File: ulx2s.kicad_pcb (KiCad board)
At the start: 4 copper layers, 35.6 x 61 mm, 27 parts, among them J1 Conn_01x24, J2 Conn_01x24, J3 Micro_SD_Card_Det, J4 USB_OTG, J5 Conn_01x06, J6 Audio-Jack-5, SW1 SW_Push, SW2 SW_Push, SW3 SW_Push, SW4 SW_Push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

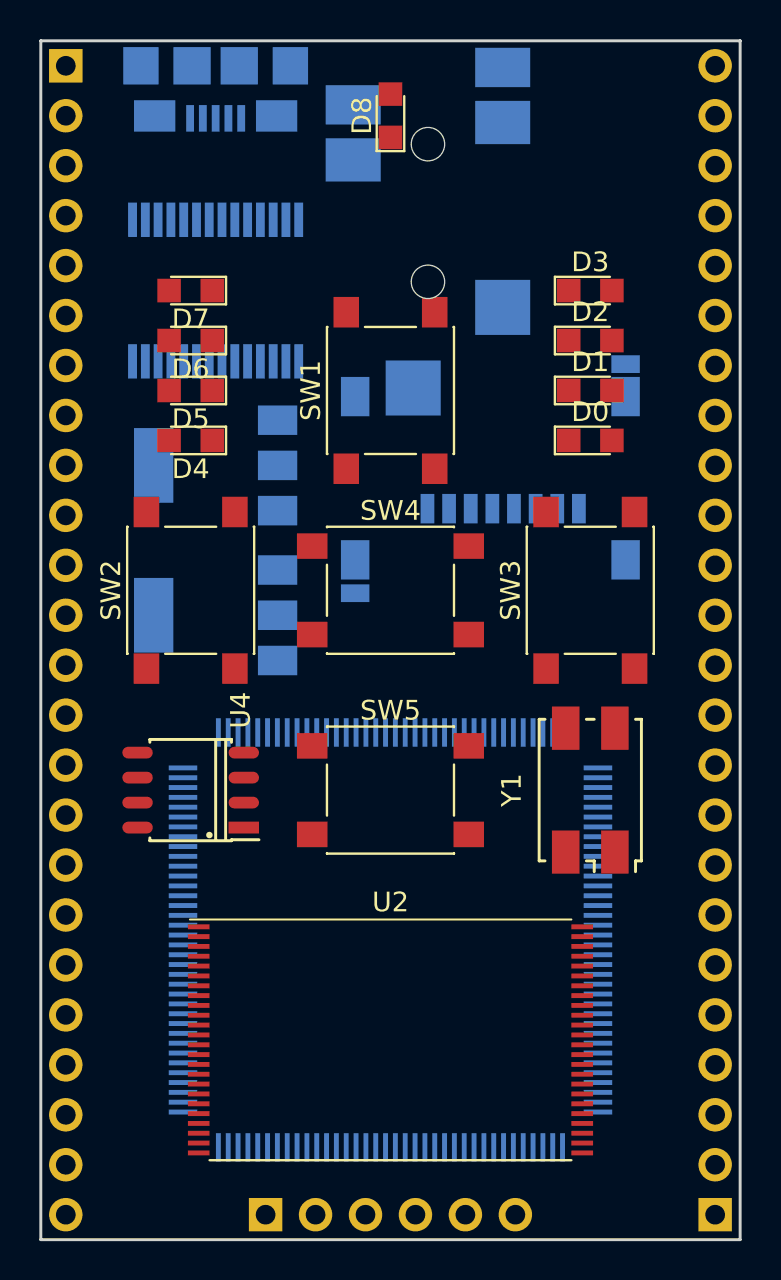
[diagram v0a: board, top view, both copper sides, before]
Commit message: moving components around to better fit
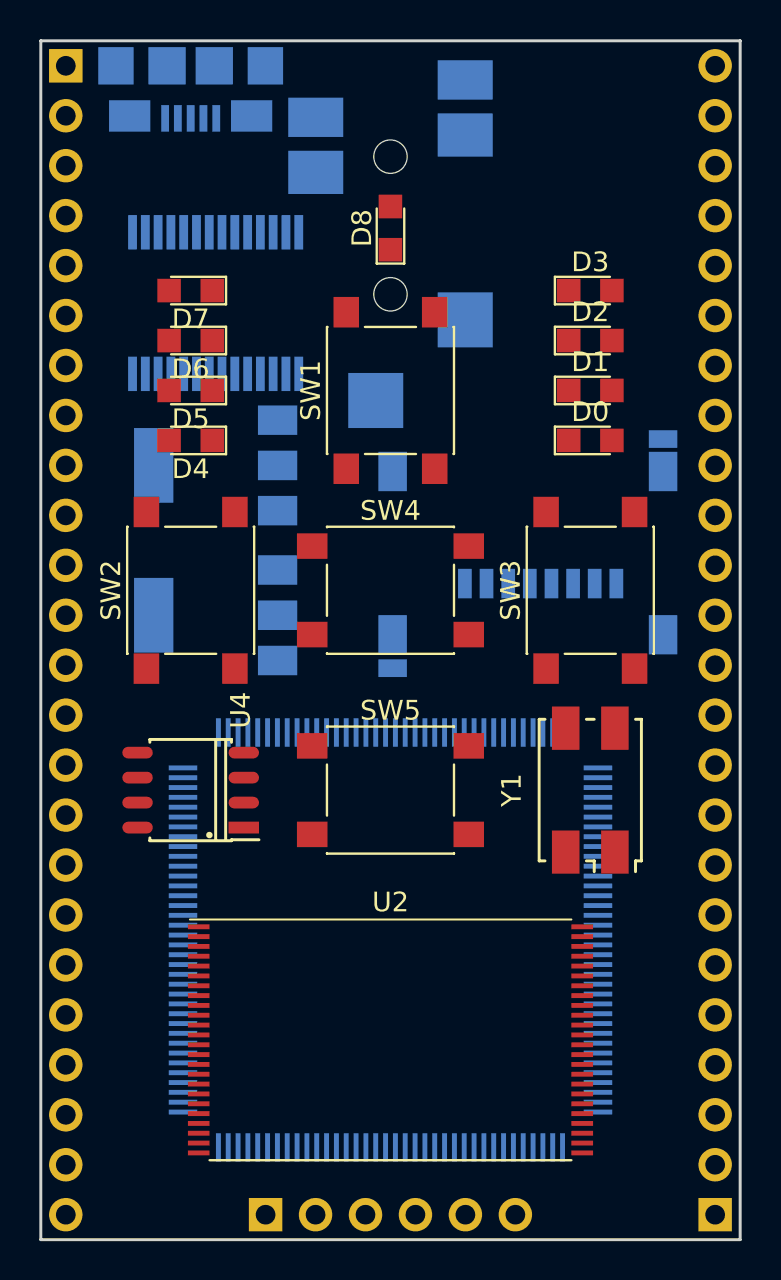
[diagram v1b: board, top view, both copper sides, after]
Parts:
- moved D8 5.72 mm to (158.8, 90.8)
- moved J3 4.26 mm to (165.7, 106.7)
- moved J6 2.01 mm to (158.8, 90.2)
- moved J4 1.27 mm to (148.6, 82.5)
- moved U3 0.63 mm to (149.9, 94.6)
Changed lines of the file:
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@@
   )
   (module micro-sd:SCHD3A100 (layer B.Cu)
-    (at 163.83 102.87 270)
+    (at 165.735 106.68 270)
     (descr "Micro SD card slot SCHD3A0100 from ALPS or ON-STARS")
     (tags "Micro SD SCHD3A0100")
@@
   )
   (module usb_otg:USB-MICRO-B-FCI-10118192-0001LF (layer B.Cu)
-    (at 149.86 82.55)
+    (at 148.59 82.55)
     (fp_text reference J4 (at 0 4.2) (layer B.SilkS)
       (effects (font (size 0.7 0.7) (thickness 0.15)) (justify mirror))
@@
   )
   (module LEDs:LED_0805 (layer F.Cu)
-    (at 158.75 85.09 90)
+    (at 158.75 90.805 90)
     (descr "LED 0805 smd package")
     (tags "LED led 0805 SMD smd SMT smt smdled SMDLED smtled SMTLED")
@@
   )
   (module Housings_SSOP:SSOP-28_5.3x10.2mm_Pitch0.65mm (layer B.Cu)
-    (at 149.86 93.98 90)
+    (at 149.86 94.615 90)
     (descr "28-Lead Plastic Shrink Small Outline (SS)-5.30 mm Body [SSOP] (see Microchip Packaging Specification 00000049BS.pdf)")
     (tags "SSOP 0.65")
     (attr smd)
-    (fp_text reference U3 (at 0 6.25 90) (layer B.SilkS)
+    (fp_text reference U3 (at 0 -5.715 90) (layer B.SilkS)
       (effects (font (size 1 1) (thickness 0.15)) (justify mirror))
     )
@@
   )
   (module audio-jack:CUI_SJ-43516-SMT (layer B.Cu)
-    (at 160.655 89.535 180)
+    (at 158.75 90.17 180)
     (descr "CUI 6-pin audio jack SMT")
     (tags "audio jack")

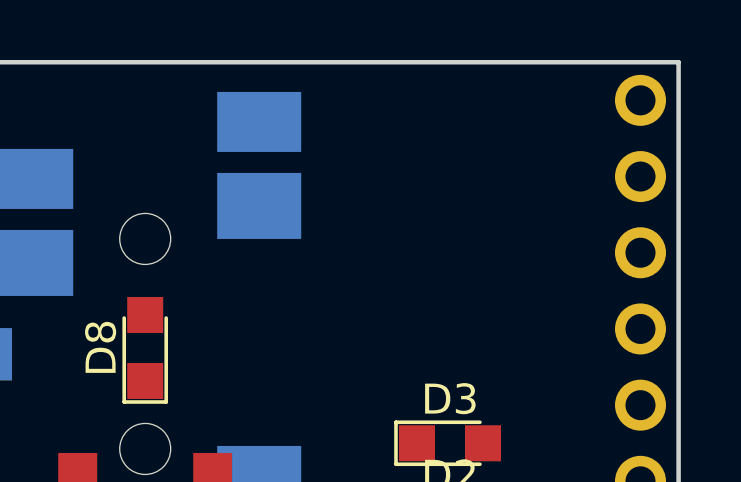
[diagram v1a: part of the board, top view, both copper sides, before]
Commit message: micro hdmi connector
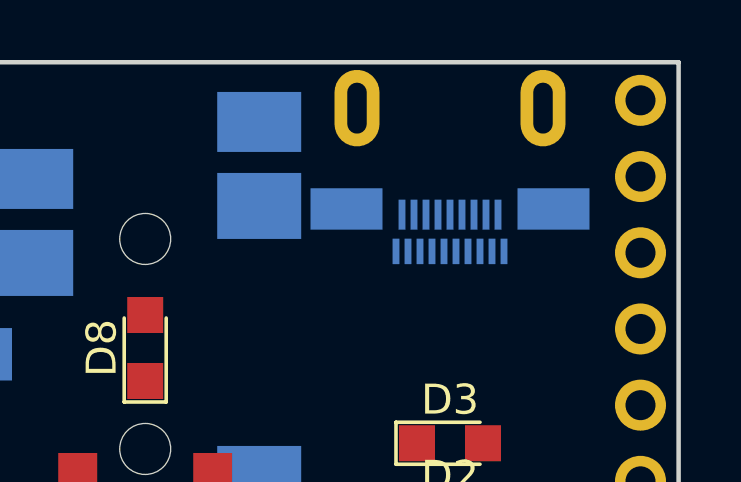
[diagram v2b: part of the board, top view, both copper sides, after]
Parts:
- added P1: MICRO-HDMI-D, micro-hdmi-d:MICRO-HDMI-D, B.Cu at (168.9, 81.1)
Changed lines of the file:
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@@
     (tracks 0)
     (zones 0)
-    (modules 27)
+    (modules 28)
     (nets 13)
   )
@@
       (clearance 0.4))
   )
+  (module micro-hdmi-d:MICRO-HDMI-D (layer B.Cu)
+    (at 168.91 81.11)
+    (attr smd)
+    (fp_text reference P1 (at -0.025 3.125) (layer B.SilkS)
+      (effects (font (size 0.3 0.3) (thickness 0.075)) (justify mirror))
+    )
+    (fp_text value MICRO-HDMI-D (at 0 1.6) (layer B.SilkS)
+      (effects (font (size 0.3 0.3) (thickness 0.075)) (justify mirror))
+    )
+    (fp_line (start -3.3 0) (end -3.3 -0.7) (layer B.SilkS) (width 0.001))
+    (fp_line (start -3.3 -0.7) (end 3.3 -0.7) (layer B.SilkS) (width 0.001))
+    (fp_line (start 3.3 -0.7) (end 3.3 0) (layer B.SilkS) (width 0.001))
+    (fp_line (start -3.3 0) (end -3.3 6.8) (layer B.SilkS) (width 0.001))
+    (fp_line (start -3.3 6.8) (end 3.3 6.8) (layer B.SilkS) (width 0.001))
+    (fp_line (start 3.3 6.8) (end 3.3 0) (layer B.SilkS) (width 0.001))
+    (fp_line (start 3.3 0) (end -3.3 0) (layer B.SilkS) (width 0.001))
+    (pad 1 smd rect (at 1.8 6.475) (size 0.23 0.85) (layers B.Cu B.Paste B.Mask))
+    (pad 3 smd rect (at 1.4 6.475) (size 0.23 0.85) (layers B.Cu B.Paste B.Mask))
+    (pad 5 smd rect (at 1 6.475) (size 0.23 0.85) (layers B.Cu B.Paste B.Mask))
+    (pad 7 smd rect (at 0.6 6.475) (size 0.23 0.85) (layers B.Cu B.Paste B.Mask))
+    (pad 9 smd rect (at 0.2 6.475) (size 0.23 0.85) (layers B.Cu B.Paste B.Mask))
+    (pad 11 smd rect (at -0.2 6.475) (size 0.23 0.85) (layers B.Cu B.Paste B.Mask))
+    (pad 13 smd rect (at -0.6 6.475) (size 0.23 0.85) (layers B.Cu B.Paste B.Mask))
+    (pad 15 smd rect (at -1 6.475) (size 0.23 0.85) (layers B.Cu B.Paste B.Mask))
+    (pad 17 smd rect (at -1.4 6.475) (size 0.23 0.85) (layers B.Cu B.Paste B.Mask))
+    (pad 19 smd rect (at -1.8 6.475) (size 0.23 0.85) (layers B.Cu B.Paste B.Mask))
+    (pad 2 smd rect (at 1.6 5.25) (size 0.23 1) (layers B.Cu B.Paste B.Mask))
+    (pad 4 smd rect (at 1.2 5.25) (size 0.23 1) (layers B.Cu B.Paste B.Mask))
+    (pad 6 smd rect (at 0.8 5.25) (size 0.23 1) (layers B.Cu B.Paste B.Mask))
+    (pad 8 smd rect (at 0.4 5.25) (size 0.23 1) (layers B.Cu B.Paste B.Mask))
+    (pad 10 smd rect (at 0 5.25) (size 0.23 1) (layers B.Cu B.Paste B.Mask))
+    (pad 12 smd rect (at -0.4 5.25) (size 0.23 1) (layers B.Cu B.Paste B.Mask))
+    (pad 14 smd rect (at -0.8 5.25) (size 0.23 1) (layers B.Cu B.Paste B.Mask))
+    (pad 16 smd rect (at -1.2 5.25) (size 0.23 1) (layers B.Cu B.Paste B.Mask))
+    (pad 18 smd rect (at -1.6 5.25) (size 0.23 1) (layers B.Cu B.Paste B.Mask))
+    (pad SHD smd rect (at 3.45 5.06) (size 2.4 1.38) (layers B.Cu B.Paste B.Mask))
+    (pad SHD smd rect (at -3.45 5.06) (size 2.4 1.38) (layers B.Cu B.Paste B.Mask))
+    (pad "" thru_hole oval (at -3.1 1.7) (size 1.5 2.55) (drill oval 0.65 1.7) (layers *.Cu *.Mask B.SilkS))
+    (pad "" thru_hole oval (at 3.1 1.7) (size 1.5 2.55) (drill oval 0.65 1.7) (layers *.Cu *.Mask B.SilkS))
+  )
   (gr_line (start 140.97 81.28) (end 140.97 142.24) (layer Edge.Cuts) (width 0.15))

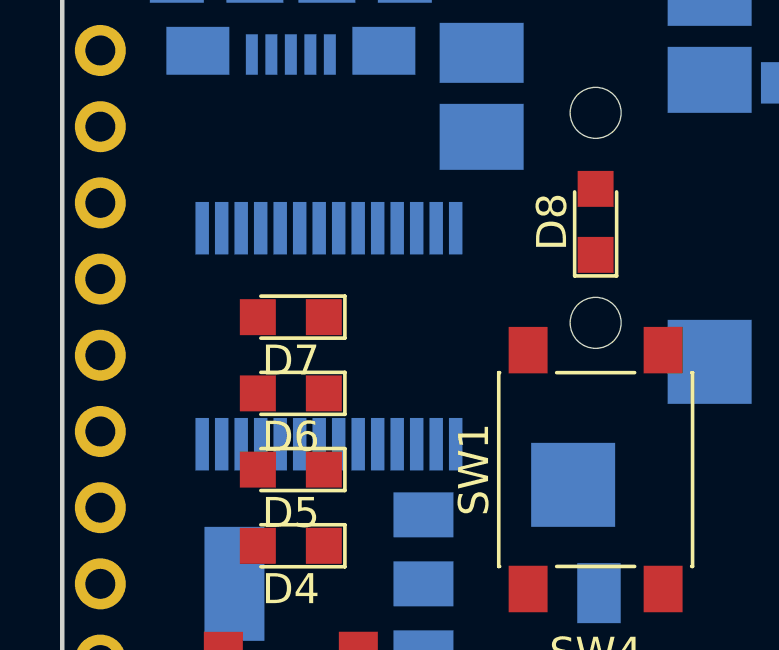
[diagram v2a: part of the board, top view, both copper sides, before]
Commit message: usbserial FT232RL changed to FT231XS
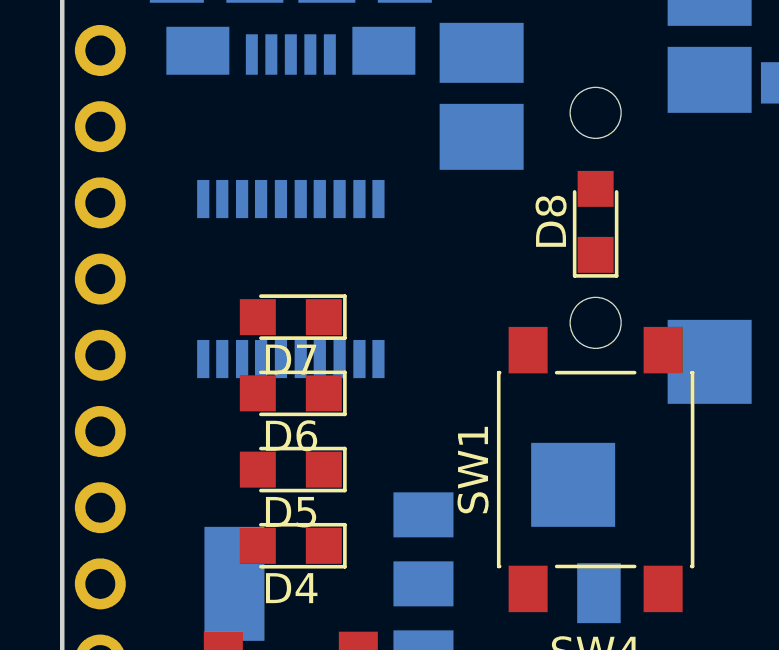
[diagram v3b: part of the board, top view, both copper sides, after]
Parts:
- U3: value FT232RL -> FT231XS; footprint Housings_SSOP:SSOP-28_5.3x10.2mm_Pitch0.65mm -> SMD_Packages:SSOP-20
- moved U3 2.29 mm to (148.6, 92.7), turned to 180 degrees
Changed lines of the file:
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@@
-    )
-  )
-  (module Housings_SSOP:SSOP-28_5.3x10.2mm_Pitch0.65mm (layer B.Cu)
-    (at 149.86 94.615 90)
-    (descr "28-Lead Plastic Shrink Small Outline (SS)-5.30 mm Body [SSOP] (see Microchip Packaging Specification 00000049BS.pdf)")
-    (tags "SSOP 0.65")
-    (attr smd)
-    (fp_text reference U3 (at 0 -5.715 90) (layer B.SilkS)
-      (effects (font (size 1 1) (thickness 0.15)) (justify mirror))
-    )
-    (fp_text value FT232RL (at 0 -6.25 90) (layer B.Fab)
-      (effects (font (size 1 1) (thickness 0.15)) (justify mirror))
-    )
-    (fp_line (start -1.65 5.1) (end 2.65 5.1) (layer B.Fab) (width 0.15))
-    (fp_line (start 2.65 5.1) (end 2.65 -5.1) (layer B.Fab) (width 0.15))
-    (fp_line (start 2.65 -5.1) (end -2.65 -5.1) (layer B.Fab) (width 0.15))
-    (fp_line (start -2.65 -5.1) (end -2.65 4.1) (layer B.Fab) (width 0.15))
-    (fp_line (start -2.65 4.1) (end -1.65 5.1) (layer B.Fab) (width 0.15))
-    (fp_line (start -4.75 5.5) (end -4.75 -5.5) (layer B.CrtYd) (width 0.05))
-    (fp_line (start 4.75 5.5) (end 4.75 -5.5) (layer B.CrtYd) (width 0.05))
-    (fp_line (start -4.75 5.5) (end 4.75 5.5) (layer B.CrtYd) (width 0.05))
-    (fp_line (start -4.75 -5.5) (end 4.75 -5.5) (layer B.CrtYd) (width 0.05))
-    (fp_line (start -2.875 5.325) (end -2.875 4.75) (layer B.SilkS) (width 0.15))
-    (fp_line (start 2.875 5.325) (end 2.875 4.675) (layer B.SilkS) (width 0.15))
-    (fp_line (start 2.875 -5.325) (end 2.875 -4.675) (layer B.SilkS) (width 0.15))
-    (fp_line (start -2.875 -5.325) (end -2.875 -4.675) (layer B.SilkS) (width 0.15))
-    (fp_line (start -2.875 5.325) (end 2.875 5.325) (layer B.SilkS) (width 0.15))
-    (fp_line (start -2.875 -5.325) (end 2.875 -5.325) (layer B.SilkS) (width 0.15))
-    (fp_line (start -2.875 4.75) (end -4.475 4.75) (layer B.SilkS) (width 0.15))
-    (fp_text user %R (at 0 0 90) (layer B.Fab)
-      (effects (font (size 0.8 0.8) (thickness 0.15)) (justify mirror))
-    )
-    (pad 1 smd rect (at -3.6 4.225 90) (size 1.75 0.45) (layers B.Cu B.Paste B.Mask))
-    (pad 2 smd rect (at -3.6 3.575 90) (size 1.75 0.45) (layers B.Cu B.Paste B.Mask))
-    (pad 3 smd rect (at -3.6 2.925 90) (size 1.75 0.45) (layers B.Cu B.Paste B.Mask))
-    (pad 4 smd rect (at -3.6 2.275 90) (size 1.75 0.45) (layers B.Cu B.Paste B.Mask))
-    (pad 5 smd rect (at -3.6 1.625 90) (size 1.75 0.45) (layers B.Cu B.Paste B.Mask))
-    (pad 6 smd rect (at -3.6 0.975 90) (size 1.75 0.45) (layers B.Cu B.Paste B.Mask))
-    (pad 7 smd rect (at -3.6 0.325 90) (size 1.75 0.45) (layers B.Cu B.Paste B.Mask))
-    (pad 8 smd rect (at -3.6 -0.325 90) (size 1.75 0.45) (layers B.Cu B.Paste B.Mask))
-    (pad 9 smd rect (at -3.6 -0.975 90) (size 1.75 0.45) (layers B.Cu B.Paste B.Mask))
-    (pad 10 smd rect (at -3.6 -1.625 90) (size 1.75 0.45) (layers B.Cu B.Paste B.Mask))
-    (pad 11 smd rect (at -3.6 -2.275 90) (size 1.75 0.45) (layers B.Cu B.Paste B.Mask))
-    (pad 12 smd rect (at -3.6 -2.925 90) (size 1.75 0.45) (layers B.Cu B.Paste B.Mask))
-    (pad 13 smd rect (at -3.6 -3.575 90) (size 1.75 0.45) (layers B.Cu B.Paste B.Mask))
-    (pad 14 smd rect (at -3.6 -4.225 90) (size 1.75 0.45) (layers B.Cu B.Paste B.Mask))
-    (pad 15 smd rect (at 3.6 -4.225 90) (size 1.75 0.45) (layers B.Cu B.Paste B.Mask))
-    (pad 16 smd rect (at 3.6 -3.575 90) (size 1.75 0.45) (layers B.Cu B.Paste B.Mask))
-    (pad 17 smd rect (at 3.6 -2.925 90) (size 1.75 0.45) (layers B.Cu B.Paste B.Mask))
-    (pad 18 smd rect (at 3.6 -2.275 90) (size 1.75 0.45) (layers B.Cu B.Paste B.Mask))
-    (pad 19 smd rect (at 3.6 -1.625 90) (size 1.75 0.45) (layers B.Cu B.Paste B.Mask))
-    (pad 20 smd rect (at 3.6 -0.975 90) (size 1.75 0.45) (layers B.Cu B.Paste B.Mask))
-    (pad 21 smd rect (at 3.6 -0.325 90) (size 1.75 0.45) (layers B.Cu B.Paste B.Mask))
-    (pad 22 smd rect (at 3.6 0.325 90) (size 1.75 0.45) (layers B.Cu B.Paste B.Mask))
-    (pad 23 smd rect (at 3.6 0.975 90) (size 1.75 0.45) (layers B.Cu B.Paste B.Mask))
-    (pad 24 smd rect (at 3.6 1.625 90) (size 1.75 0.45) (layers B.Cu B.Paste B.Mask))
-    (pad 25 smd rect (at 3.6 2.275 90) (size 1.75 0.45) (layers B.Cu B.Paste B.Mask))
-    (pad 26 smd rect (at 3.6 2.925 90) (size 1.75 0.45) (layers B.Cu B.Paste B.Mask))
-    (pad 27 smd rect (at 3.6 3.575 90) (size 1.75 0.45) (layers B.Cu B.Paste B.Mask))
-    (pad 28 smd rect (at 3.6 4.225 90) (size 1.75 0.45) (layers B.Cu B.Paste B.Mask))
-    (model ${KISYS3DMOD}/Housings_SSOP.3dshapes/SSOP-28_5.3x10.2mm_Pitch0.65mm.wrl
-      (at (xyz 0 0 0))
-      (scale (xyz 1 1 1))
-      (rotate (xyz 0 0 0))
     )
   )
@@
     (pad "" thru_hole oval (at 3.1 1.7) (size 1.5 2.55) (drill oval 0.65 1.7) (layers *.Cu *.Mask B.SilkS))
   )
+  (module SMD_Packages:SSOP-20 (layer B.Cu)
+    (at 148.59 92.71 180)
+    (descr "SSOP 20 pins")
+    (tags "CMS SSOP SMD")
+    (attr smd)
+    (fp_text reference U3 (at 0 0.635 180) (layer B.SilkS)
+      (effects (font (size 1 1) (thickness 0.15)) (justify mirror))
+    )
+    (fp_text value FT231XS (at 0 -0.635 180) (layer B.Fab)
+      (effects (font (size 1 1) (thickness 0.15)) (justify mirror))
+    )
+    (fp_line (start 3.81 1.778) (end -3.81 1.778) (layer B.SilkS) (width 0.15))
+    (fp_line (start -3.81 -1.778) (end 3.81 -1.778) (layer B.SilkS) (width 0.15))
+    (fp_line (start 3.81 1.778) (end 3.81 -1.778) (layer B.SilkS) (width 0.15))
+    (fp_line (start -3.81 -1.778) (end -3.81 1.778) (layer B.SilkS) (width 0.15))
+    (fp_circle (center -3.302 -1.27) (end -3.556 -1.016) (layer B.SilkS) (width 0.15))
+    (fp_line (start -3.81 0.635) (end -3.048 0.635) (layer B.SilkS) (width 0.15))
+    (fp_line (start -3.048 0.635) (end -3.048 -0.635) (layer B.SilkS) (width 0.15))
+    (fp_line (start -3.048 -0.635) (end -3.81 -0.635) (layer B.SilkS) (width 0.15))
+    (pad 1 smd rect (at -2.921 -2.667 180) (size 0.4064 1.27) (layers B.Cu B.Paste B.Mask))
+    (pad 2 smd rect (at -2.286 -2.667 180) (size 0.4064 1.27) (layers B.Cu B.Paste B.Mask))
+    (pad 3 smd rect (at -1.6256 -2.667 180) (size 0.4064 1.27) (layers B.Cu B.Paste B.Mask))
+    (pad 4 smd rect (at -0.9652 -2.667 180) (size 0.4064 1.27) (layers B.Cu B.Paste B.Mask))
+    (pad 5 smd rect (at -0.3302 -2.667 180) (size 0.4064 1.27) (layers B.Cu B.Paste B.Mask))
+    (pad 6 smd rect (at 0.3302 -2.667 180) (size 0.4064 1.27) (layers B.Cu B.Paste B.Mask))
+    (pad 7 smd rect (at 0.9906 -2.667 180) (size 0.4064 1.27) (layers B.Cu B.Paste B.Mask))
+    (pad 8 smd rect (at 1.6256 -2.667 180) (size 0.4064 1.27) (layers B.Cu B.Paste B.Mask))
+    (pad 9 smd rect (at 2.286 -2.667 180) (size 0.4064 1.27) (layers B.Cu B.Paste B.Mask))
+    (pad 10 smd rect (at 2.921 -2.667 180) (size 0.4064 1.27) (layers B.Cu B.Paste B.Mask))
+    (pad 11 smd rect (at 2.921 2.667 180) (size 0.4064 1.27) (layers B.Cu B.Paste B.Mask))
+    (pad 12 smd rect (at 2.286 2.667 180) (size 0.4064 1.27) (layers B.Cu B.Paste B.Mask))
+    (pad 13 smd rect (at 1.6256 2.667 180) (size 0.4064 1.27) (layers B.Cu B.Paste B.Mask))
+    (pad 14 smd rect (at 0.9906 2.667 180) (size 0.4064 1.27) (layers B.Cu B.Paste B.Mask))
+    (pad 15 smd rect (at 0.3302 2.667 180) (size 0.4064 1.27) (layers B.Cu B.Paste B.Mask))
+    (pad 16 smd rect (at -0.3302 2.667 180) (size 0.4064 1.27) (layers B.Cu B.Paste B.Mask))
+    (pad 17 smd rect (at -0.9652 2.667 180) (size 0.4064 1.27) (layers B.Cu B.Paste B.Mask))
+    (pad 18 smd rect (at -1.6256 2.667 180) (size 0.4064 1.27) (layers B.Cu B.Paste B.Mask))
+    (pad 19 smd rect (at -2.286 2.667 180) (size 0.4064 1.27) (layers B.Cu B.Paste B.Mask))
+    (pad 20 smd rect (at -2.921 2.667 180) (size 0.4064 1.27) (layers B.Cu B.Paste B.Mask))
+    (model SMD_Packages.3dshapes/SSOP-20.wrl
+      (at (xyz 0 0 0))
+      (scale (xyz 0.255 0.33 0.3))
+      (rotate (xyz 0 0 0))
+    )
+  )
   (gr_line (start 140.97 81.28) (end 140.97 142.24) (layer Edge.Cuts) (width 0.15))
